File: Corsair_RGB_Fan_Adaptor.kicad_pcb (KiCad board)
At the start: 2 copper layers, 63.5 x 38.1 mm, 7 parts, among them J1 Mobo, J2 Fan1, J3 Fan2, J4 Fan3, J5 Fan4, J6 Fan5, J7 Fan6

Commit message: Filter Capacitor
Adding filter capacitor to board for smoothing 5V power input.
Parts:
- added C1: CP, Capacitor_THT:CP_Radial_D6.3mm_P2.50mm, F.Cu at (121.9, 119.4)

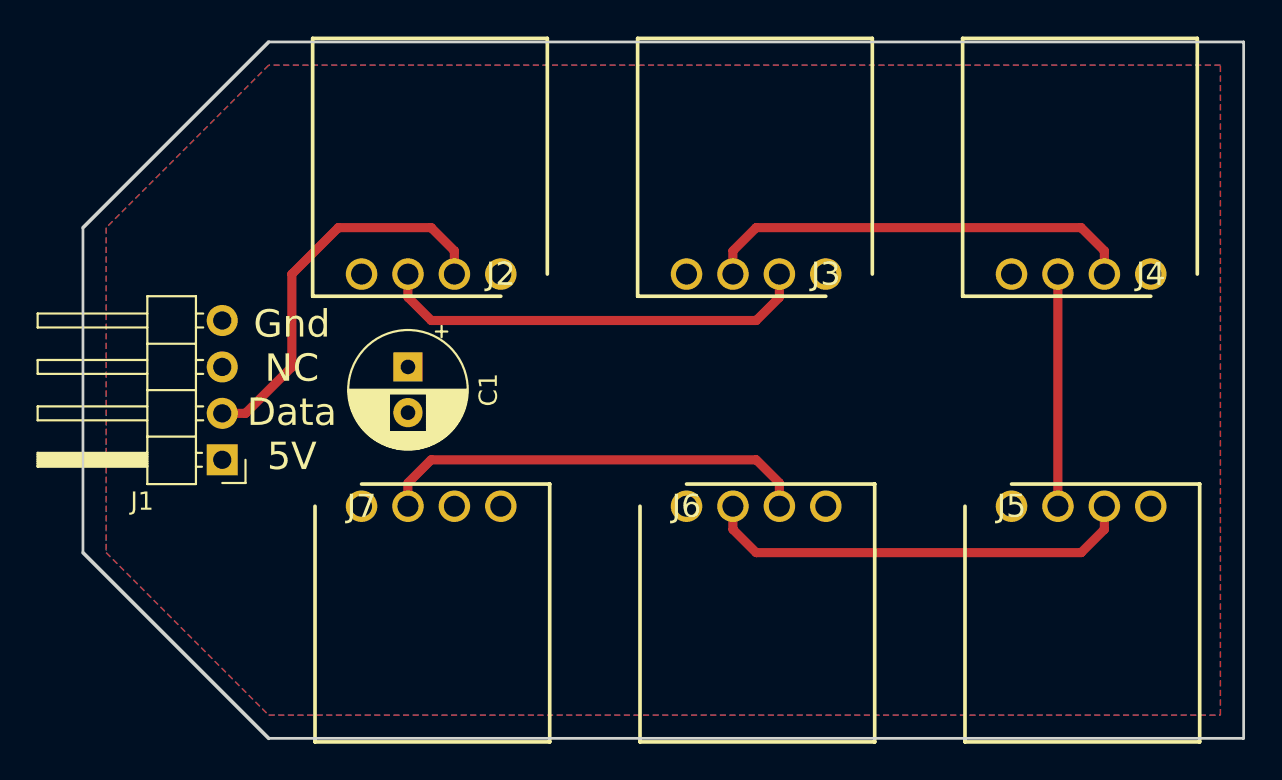
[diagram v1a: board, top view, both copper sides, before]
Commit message: added some labeling to the PCB
Added labels for numbering and locations
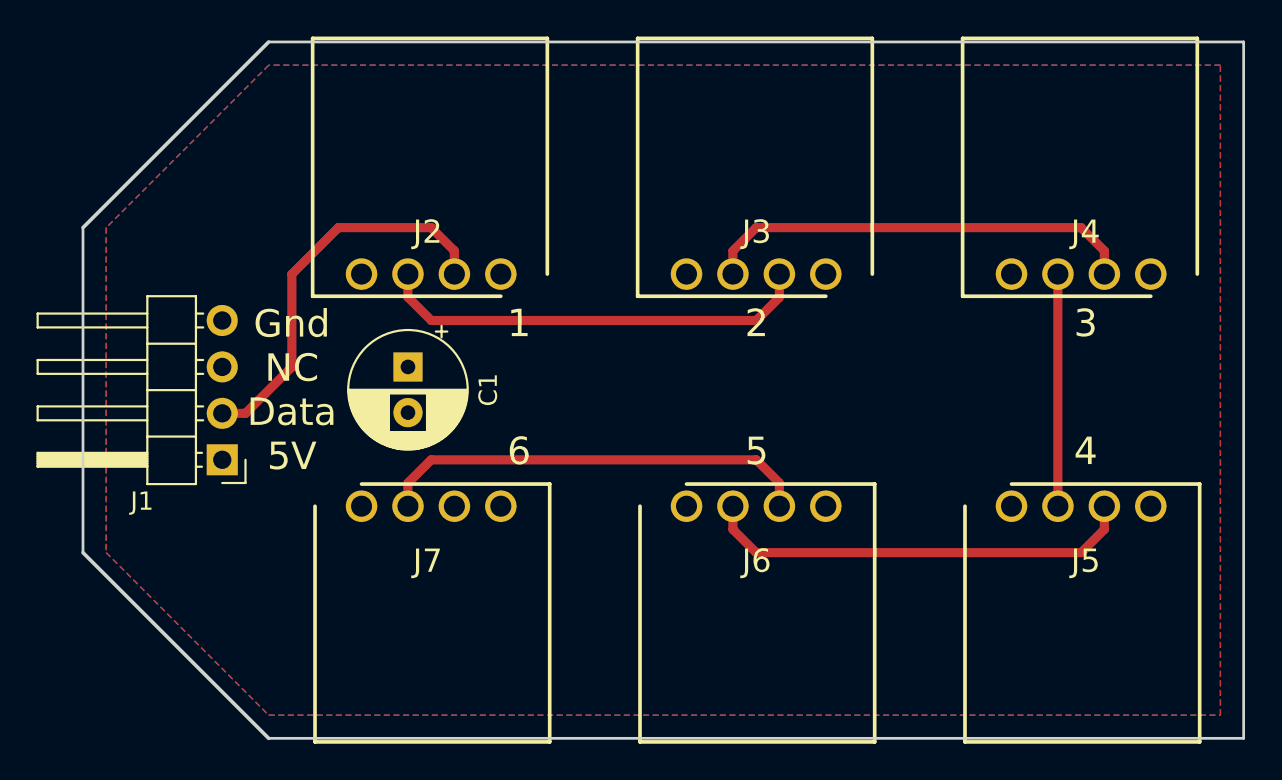
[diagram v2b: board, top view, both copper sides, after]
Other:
- board text added: "1"
- board text added: "2"
- board text added: "3"
- board text added: "4"
- board text added: "5"
- board text added: "6"
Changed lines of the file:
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@@
-(kicad_pcb (version 20171130) (host pcbnew "(5.0.0)")
+(kicad_pcb (version 20171130) (host pcbnew "(5.1.4)-1")
   (general
     (thickness 1.6)
-    (drawings 7)
+    (drawings 13)
     (tracks 28)
     (zones 0)
@@
     (zone_45_only no)
     (trace_min 0.2)
-    (segment_width 0.2)
-    (edge_width 0.15)
     (via_size 0.8)
     (via_drill 0.4)
@@
     (uvia_min_size 0.2)
     (uvia_min_drill 0.1)
+    (edge_width 0.15)
+    (segment_width 0.2)
     (pcb_text_width 0.3)
     (pcb_text_size 1.5 1.5)
@@
     (descr 70553-0003)
     (tags Connector)
-    (fp_text reference J2 (at 0 0 180) (layer F.SilkS)
-      (effects (font (size 1.27 1.27) (thickness 0.254)))
-    )
-    (fp_text value Fan1 (at 0 0 180) (layer F.SilkS) hide
+    (fp_text reference J2 (at 4 2.3 180) (layer F.SilkS)
+      (effects (font (size 1.27 1.27) (thickness 0.254)))
+    )
+    (fp_text value Fan1 (at 4 6.3 180) (layer F.SilkS) hide
       (effects (font (size 1.27 1.27) (thickness 0.254)))
     )
@@
     (descr 70553-0003)
     (tags Connector)
-    (fp_text reference J3 (at 0 0 180) (layer F.SilkS)
-      (effects (font (size 1.27 1.27) (thickness 0.254)))
-    )
-    (fp_text value Fan2 (at 0 0 180) (layer F.SilkS) hide
+    (fp_text reference J3 (at 3.78 2.3 180) (layer F.SilkS)
+      (effects (font (size 1.27 1.27) (thickness 0.254)))
+    )
+    (fp_text value Fan2 (at 3.78 6.3 180) (layer F.SilkS) hide
       (effects (font (size 1.27 1.27) (thickness 0.254)))
     )
@@
     (descr 70553-0003)
     (tags Connector)
-    (fp_text reference J4 (at 0 0 180) (layer F.SilkS)
-      (effects (font (size 1.27 1.27) (thickness 0.254)))
-    )
-    (fp_text value Fan3 (at 0 0 180) (layer F.SilkS) hide
+    (fp_text reference J4 (at 3.56 2.3 180) (layer F.SilkS)
+      (effects (font (size 1.27 1.27) (thickness 0.254)))
+    )
+    (fp_text value Fan3 (at 3.56 6.3 180) (layer F.SilkS) hide
       (effects (font (size 1.27 1.27) (thickness 0.254)))
     )
@@
     (descr 70553-0003)
     (tags Connector)
-    (fp_text reference J5 (at 0 0) (layer F.SilkS)
-      (effects (font (size 1.27 1.27) (thickness 0.254)))
-    )
-    (fp_text value Fan4 (at 0 0) (layer F.SilkS) hide
+    (fp_text reference J5 (at 4.06 3) (layer F.SilkS)
+      (effects (font (size 1.27 1.27) (thickness 0.254)))
+    )
+    (fp_text value Fan4 (at 4.06 6) (layer F.SilkS) hide
       (effects (font (size 1.27 1.27) (thickness 0.254)))
     )
@@
     (descr 70553-0003)
     (tags Connector)
-    (fp_text reference J6 (at 0 0) (layer F.SilkS)
-      (effects (font (size 1.27 1.27) (thickness 0.254)))
-    )
-    (fp_text value Fan5 (at 0 0) (layer F.SilkS) hide
+    (fp_text reference J6 (at 3.84 3) (layer F.SilkS)
+      (effects (font (size 1.27 1.27) (thickness 0.254)))
+    )
+    (fp_text value Fan5 (at 3.84 6) (layer F.SilkS) hide
       (effects (font (size 1.27 1.27) (thickness 0.254)))
     )
@@
     (descr 70553-0003)
     (tags Connector)
-    (fp_text reference J7 (at 0 0) (layer F.SilkS)
-      (effects (font (size 1.27 1.27) (thickness 0.254)))
-    )
-    (fp_text value Fan6 (at 0 0) (layer F.SilkS) hide
+    (fp_text reference J7 (at 3.62 3) (layer F.SilkS)
+      (effects (font (size 1.27 1.27) (thickness 0.254)))
+    )
+    (fp_text value Fan6 (at 3.62 6) (layer F.SilkS) hide
       (effects (font (size 1.27 1.27) (thickness 0.254)))
     )
@@
     )
   )
+  (gr_text 6 (at 128 124) (layer F.SilkS)
+    (effects (font (size 1.5 1.5) (thickness 0.3)))
+  )
+  (gr_text 2 (at 141 117) (layer F.SilkS)
+    (effects (font (size 1.5 1.5) (thickness 0.3)))
+  )
+  (gr_text 5 (at 141 124) (layer F.SilkS)
+    (effects (font (size 1.5 1.5) (thickness 0.3)))
+  )
+  (gr_text 4 (at 159 124) (layer F.SilkS)
+    (effects (font (size 1.5 1.5) (thickness 0.3)))
+  )
+  (gr_text "3\n" (at 159 117) (layer F.SilkS)
+    (effects (font (size 1.5 1.5) (thickness 0.3)))
+  )
+  (gr_text 1 (at 128 117) (layer F.SilkS)
+    (effects (font (size 1.5 1.5) (thickness 0.3)))
+  )
   (gr_text "Gnd\nNC\nData\n5V\n" (at 115.57 120.65) (layer F.SilkS)
